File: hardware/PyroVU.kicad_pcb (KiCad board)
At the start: 2 copper layers, 48 parts, among them IC1 TM1637__SOP_, J1 Screw_Terminal_01x05, J10 Screw_Terminal_01x09, J11 Screw_Terminal_01x09, J12 Screw_Terminal_01x09, J2 Screw_Terminal_01x02, J3 Conn_01x09_Pin, J4 Conn_01x02_Pin, J5 Conn_01x02_Pin, J6 Conn_01x02_Pin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

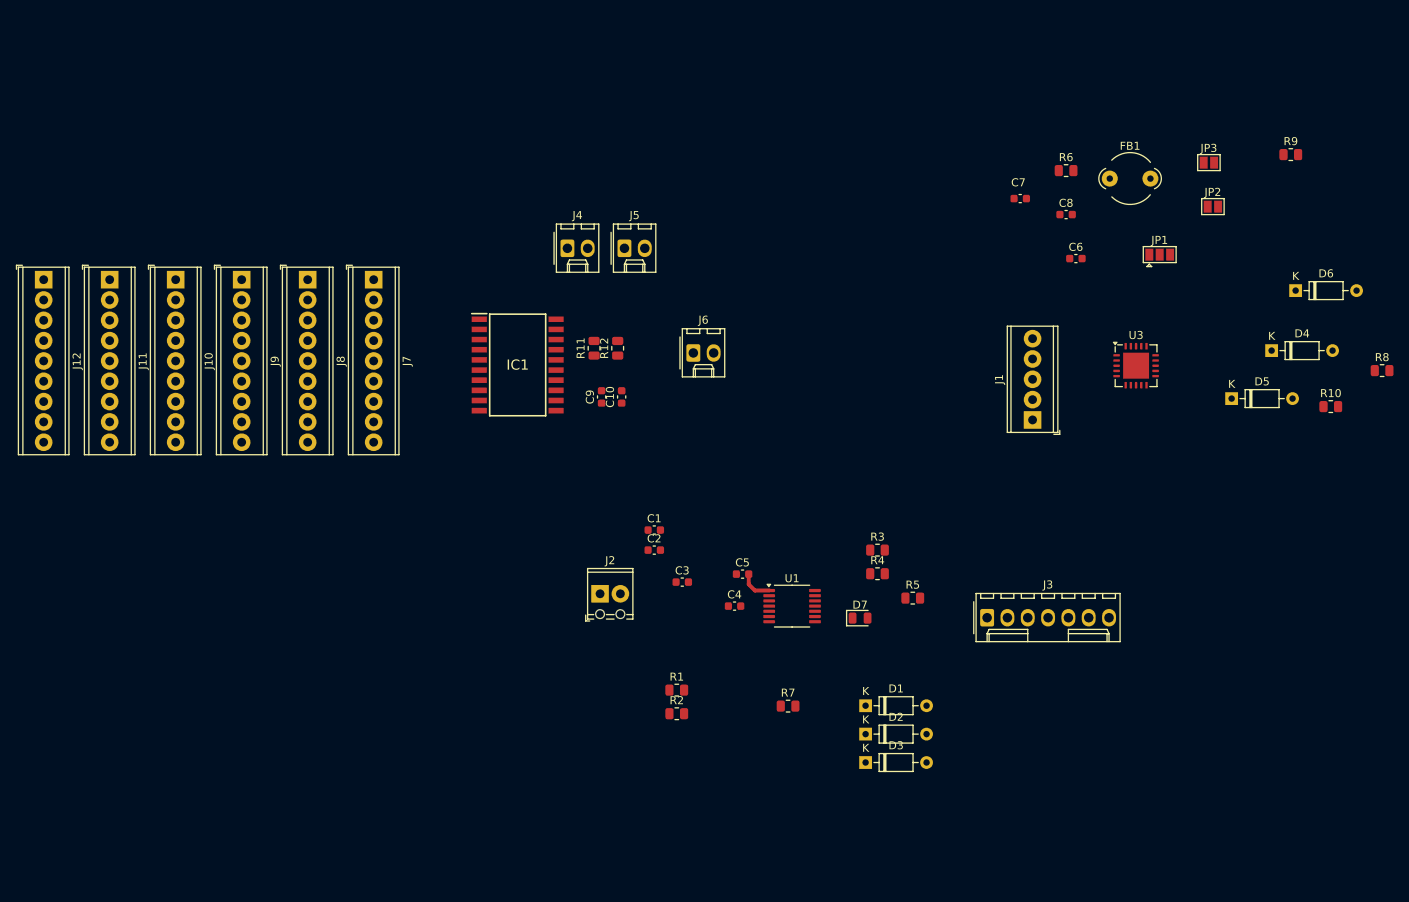
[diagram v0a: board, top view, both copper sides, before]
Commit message: Updated the schematic and added 7seg display
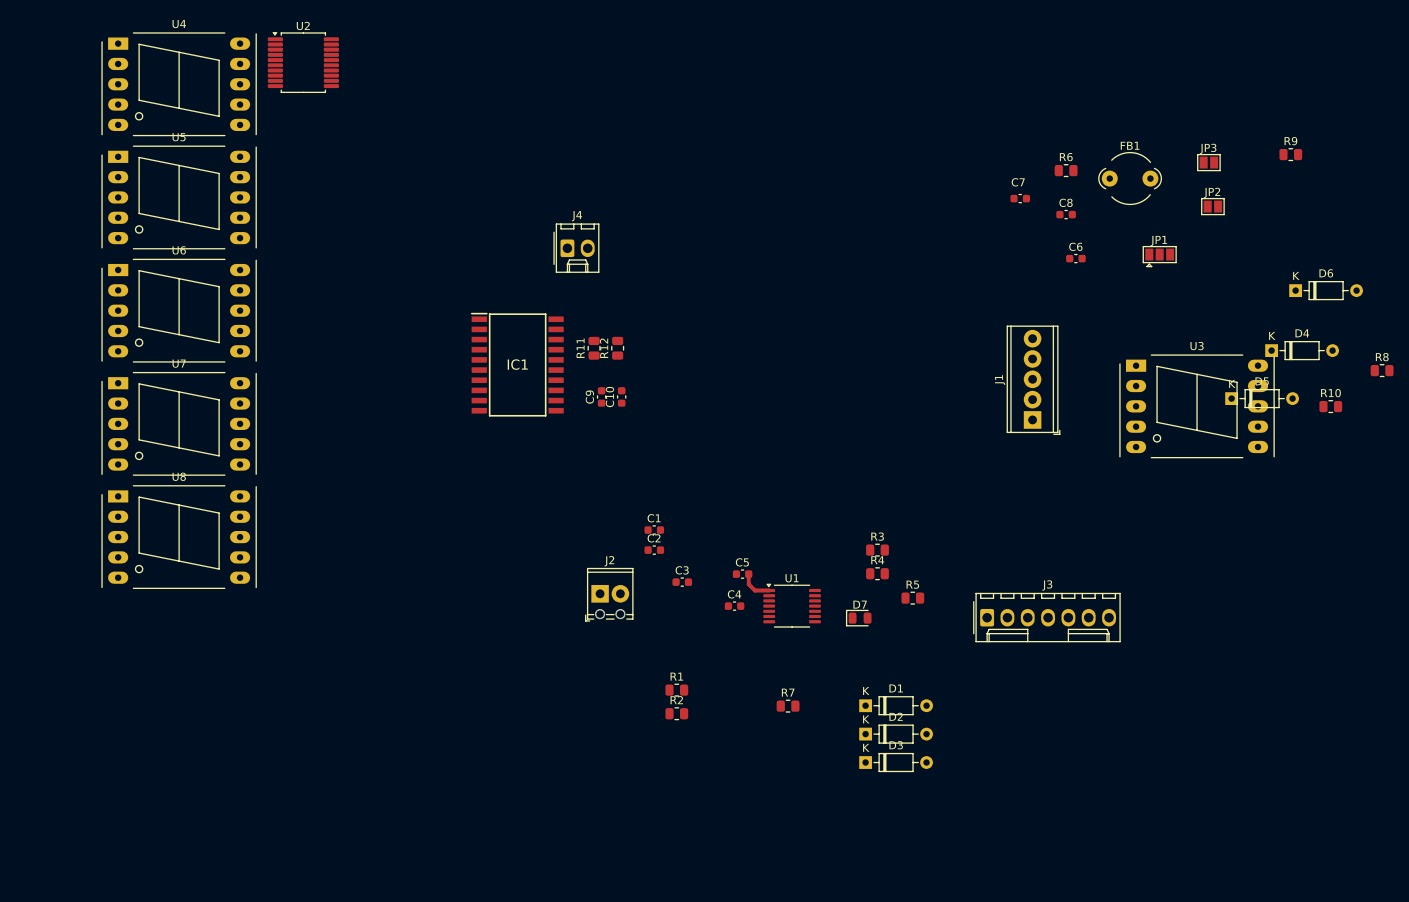
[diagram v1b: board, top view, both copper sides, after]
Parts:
- removed J10, J11, J12, J7, J8, J9: Screw_Terminal_01x09, TerminalBlock_Phoenix:TerminalBlock_Phoenix_MPT-0,5-9-2.54_1x09_P2.54mm_Horizontal
- removed J5, J6: Conn_01x02_Pin, Connector_Molex:Molex_KK-254_AE-6410-02A_1x02_P2.54mm_Vertical
- added U2: MAX31865xAP, Package_SO:SSOP-20_5.3x7.2mm_P0.65mm, F.Cu at (95.4, 35.1)
- added U4: SM420561N, Display_7Segment:7SegmentLED_LTS6760_LTS6780, F.Cu at (72.3, 32.7)
- added U5: SM420561N, Display_7Segment:7SegmentLED_LTS6760_LTS6780, F.Cu at (72.3, 46.9)
- added U6: SM420561N, Display_7Segment:7SegmentLED_LTS6760_LTS6780, F.Cu at (72.3, 61.0)
- added U7: SM420561N, Display_7Segment:7SegmentLED_LTS6760_LTS6780, F.Cu at (72.3, 75.2)
- added U8: SM420561N, Display_7Segment:7SegmentLED_LTS6760_LTS6780, F.Cu at (72.3, 89.3)
- U3: value MAX31865xTP -> SM420561N; footprint Package_DFN_QFN:TQFN-20-1EP_5x5mm_P0.65mm_EP3.25x3.25mm -> Display_7Segment:7SegmentLED_LTS6760_LTS6780
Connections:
- net Net-(IC1-CLK) renamed /CLK
- net Net-(IC1-DIO) renamed /DIO
- C6 pad 1: Net-(J4-Pin_1) -> Net-(J3-Pin_2)
- C6 pad 2: Net-(J5-Pin_2) -> Net-(J4-Pin_1)
- C8 pad 2: Net-(U3-VDD) -> Net-(U2-VDD)
- D1 pad 1: Net-(D1-K) -> /CST
- D2 pad 1: Net-(D2-K) -> /SCK
- D3 pad 1: Net-(D3-K) -> /SDI
- D4 pad 1: /CS -> /CSR
- FB1 pad 2: Net-(U3-VDD) -> Net-(U2-VDD)
- JP1 pad 1: Net-(J4-Pin_2) -> Net-(J3-Pin_1)
- JP2 pad 1: Net-(J4-Pin_1) -> Net-(J3-Pin_2)
- JP2 pad 2: Net-(J4-Pin_2) -> Net-(J3-Pin_1)
- JP3 pad 1: Net-(J5-Pin_1) -> Net-(J4-Pin_2)
- JP3 pad 2: Net-(J5-Pin_2) -> Net-(J4-Pin_1)
- R6 pad 1: Net-(U3-ISENSOR) -> Net-(U2-ISENSOR)
- R6 pad 2: Net-(U3-BIAS) -> Net-(U2-BIAS)
- U1 pad 11: Net-(J3-Pin_5) -> /SDO
- U1 pad 7: /DRDY1 -> /DRDY
- U3 pad 1: Net-(U3-BIAS) -> /SEG5
- U3 pad 10: GND -> /SEG7
- U3 pad 2: Net-(U3-BIAS) -> /SEG4
- U3 pad 3: Net-(U3-ISENSOR) -> /GRID3
- U3 pad 4: Net-(U3-ISENSOR) -> /SEG3
- U3 pad 5: Net-(J4-Pin_2) -> /SEG8
- U3 pad 6: Net-(JP1-C) -> /SEG2
- U3 pad 7: Net-(J4-Pin_1) -> /SEG1
- U3 pad 8: Net-(J5-Pin_2) -> /GRID3
- U3 pad 9: Net-(J5-Pin_1) -> /SEG6

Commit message: Changes in the Schematic
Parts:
- removed J3: Conn_01x09_Pin, Connector_Molex:Molex_KK-254_AE-6410-07A_1x07_P2.54mm_Vertical
- moved U5 117.2 mm to (179.4, 94.4)
- moved U4 117.2 mm to (179.4, 80.2)
- moved U2 98.8 mm to (156.5, 112.8)
- moved R9 87.6 mm to (155.6, 107.2)
- moved JP2 87.2 mm to (151.7, 118.8)
- moved R8 81.0 mm to (155.5, 104.8)
- moved JP1 79.7 mm to (148.5, 117.8), turned to -90 degrees
- moved JP3 78.9 mm to (165.7, 113.8)
- moved R6 77.1 mm to (148.0, 112.8), turned to 90 degrees
- moved D4 76.2 mm to (146.7, 101.8)
- moved D6 75.9 mm to (173.5, 124.1), turned to 90 degrees
- moved J4 70.7 mm to (173.5, 112.8), turned to 90 degrees
- moved C7 67.2 mm to (150.5, 109.8), turned to -90 degrees
- moved R10 65.5 mm to (167.0, 110.8), turned to 180 degrees
- moved C6 64.3 mm to (162.5, 116.8), turned to 90 degrees
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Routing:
- net +3.3V: track 0.00 -> 77.0 mm, vias 0 -> 2
- net Net-(J3-Pin_2): track 0.00 -> 18.7 mm
- net Net-(J4-Pin_1): track 0.00 -> 17.3 mm, vias 0 -> 1
- net /DRDY: track 0.00 -> 16.9 mm, vias 0 -> 1
- net Net-(J4-Pin_2): track 0.00 -> 16.1 mm
- net Net-(D2-A): track 0.00 -> 15.3 mm
- net Net-(D4-A): track 0.00 -> 14.8 mm
- net Net-(J3-Pin_1): track 0.00 -> 13.3 mm
- net GND: track 4.15 -> 16.8 mm
- net Net-(U2-VDD): track 0.00 -> 12.6 mm
- net Net-(D5-A): track 0.00 -> 11.3 mm
- net Net-(D1-A): track 0.00 -> 10.3 mm
- net Net-(D6-A): track 0.00 -> 9.70 mm
- net Net-(D3-A): track 0.00 -> 9.54 mm
- net Net-(U1-T-): track 0.00 -> 8.28 mm
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- added copper zone on F.Cu, net GND
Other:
- board outline added: 79.5 x 75.5 mm
